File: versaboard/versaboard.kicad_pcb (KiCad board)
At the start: 4 copper layers, 57 x 43 mm, 23 parts, among them J3 UART, J39 Conn_02x20_Odd_Even, J4 DBG, J40 Conn_02x20_Odd_Even, SW1 RST, U1 ATSAML21G18B-AUT, Y1 32.768kHz

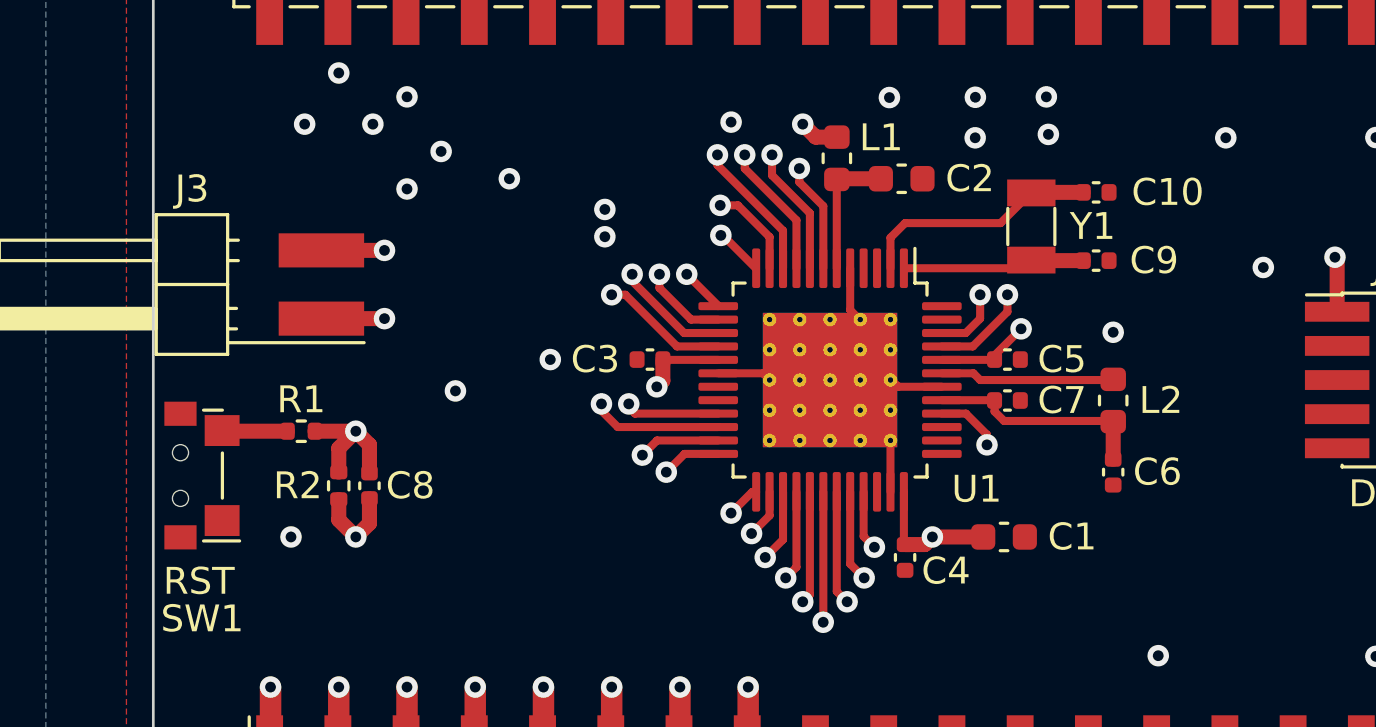
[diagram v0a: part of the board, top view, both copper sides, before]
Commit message: versaboard: geographic reannotate
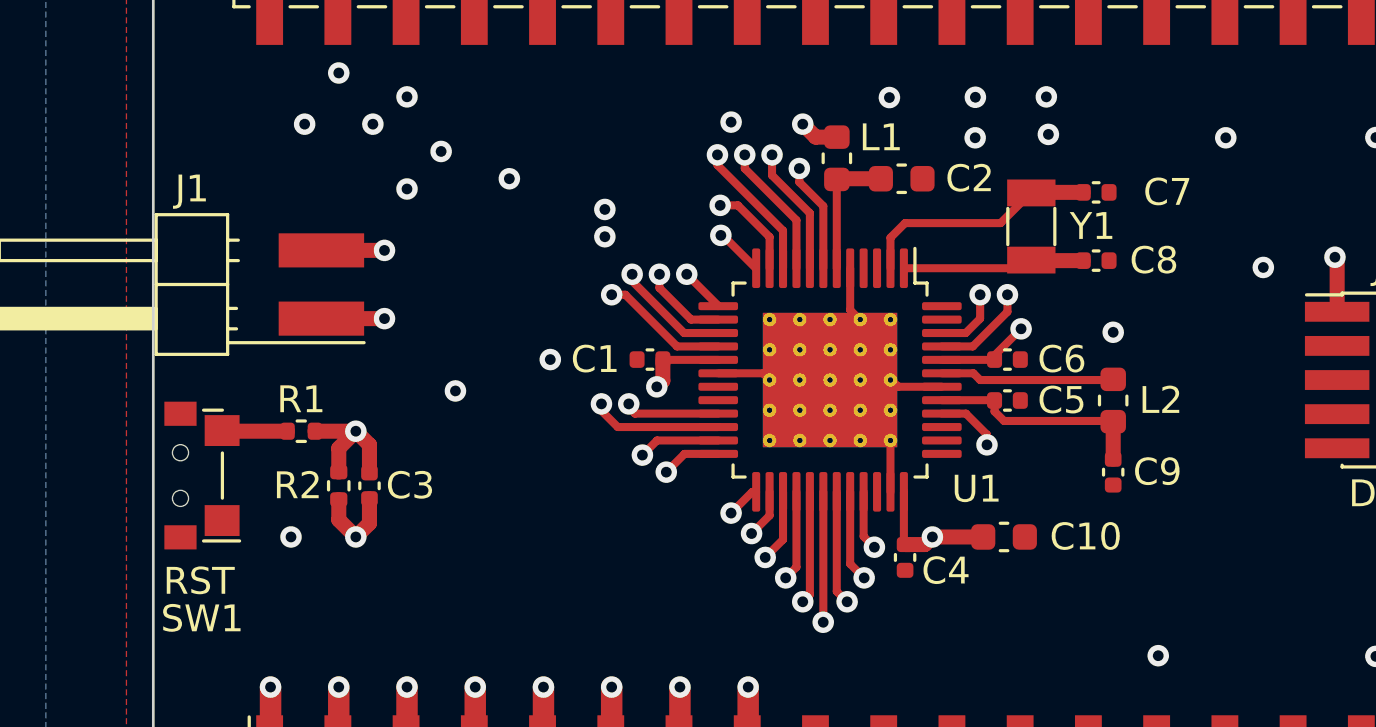
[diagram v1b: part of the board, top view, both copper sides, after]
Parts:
- renumbered C3 to C1, C1 to C10, C8 to C3, C7 to C5, C5 to C6, C10 to C7, C9 to C8, C6 to C9, J3 to J1
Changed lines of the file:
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@@
   (net 27 "/TX")
   (net 28 "/RX")
-  (net 29 "unconnected-(J4-Pad6)")
-  (net 30 "unconnected-(J4-Pad7)")
-  (net 31 "unconnected-(J4-Pad8)")
-  (net 32 "unconnected-(J4-Pad9)")
+  (net 29 "Net-(C5-Pad2)")
+  (net 30 "Net-(C6-Pad2)")
+  (net 31 "unconnected-(J3-Pad6)")
+  (net 32 "unconnected-(J3-Pad7)")
   (net 33 "/VSW")
   (net 34 "Net-(R1-Pad1)")
@@
   (net 43 "unconnected-(U1-Pad47)")
   (net 44 "unconnected-(U1-Pad48)")
-  (net 45 "Net-(C9-Pad2)")
-  (net 46 "Net-(C10-Pad2)")
+  (net 45 "unconnected-(J3-Pad8)")
+  (net 46 "unconnected-(J3-Pad9)")
   (net 47 "/SWDIO")
   (net 48 "/SWCLK")
@@
     (property "Sheetname" "")
     (attr smd)
-    (fp_text reference "C3" (at 2.032 0) (layer "F.SilkS")
+    (fp_text reference "C1" (at 2.032 0) (layer "F.SilkS")
       (effects (font (size 1 1) (thickness 0.15)))
     )
@@
     (property "Sheetname" "")
     (attr smd)
-    (fp_text reference "C7" (at 2.032 0) (layer "F.SilkS")
+    (fp_text reference "C5" (at 2.032 0) (layer "F.SilkS")
       (effects (font (size 1 1) (thickness 0.15)))
     )
@@
     (property "Sheetname" "")
     (attr smd)
-    (fp_text reference "C6" (at 0 -1.651 180) (layer "F.SilkS")
+    (fp_text reference "C9" (at 0 -1.651 180) (layer "F.SilkS")
       (effects (font (size 1 1) (thickness 0.15)))
     )
@@
     (property "Sheetname" "")
     (attr smd)
-    (fp_text reference "C5" (at 2.032 0) (layer "F.SilkS")
+    (fp_text reference "C6" (at 2.032 0) (layer "F.SilkS")
       (effects (font (size 1 1) (thickness 0.15)))
     )
@@
     (property "Sheetname" "")
     (attr smd)
-    (fp_text reference "C8" (at 0 1.524 180) (layer "F.SilkS")
+    (fp_text reference "C3" (at 0 1.524 180) (layer "F.SilkS")
       (effects (font (size 1 1) (thickness 0.15)))
     )
@@
     (fp_line (start 1.6 -0.75) (end 1.6 0.75) (layer "F.Fab") (width 0.1))
     (pad "1" smd rect (at 1.25 0 90) (size 1 1.8) (layers "F.Cu" "F.Paste" "F.Mask")
-      (net 46 "Net-(C10-Pad2)") (pinfunction "1") (pintype "passive"))
+      (net 29 "Net-(C5-Pad2)") (pinfunction "1") (pintype "passive"))
     (pad "2" smd rect (at -1.25 0 90) (size 1 1.8) (layers "F.Cu" "F.Paste" "F.Mask")
-      (net 45 "Net-(C9-Pad2)") (pinfunction "2") (pintype "passive"))
+      (net 30 "Net-(C6-Pad2)") (pinfunction "2") (pintype "passive"))
     (model "${KICAD6_3DMODEL_DIR}/Crystal.3dshapes/Crystal_SMD_3215-2Pin_3.2x1.5mm.wrl"
       (offset (xyz 0 0 0))
@@
     (property "Sheetname" "")
     (attr smd)
-    (fp_text reference "C1" (at 2.54 0 180) (layer "F.SilkS")
+    (fp_text reference "C10" (at 3.048 0 180) (layer "F.SilkS")
       (effects (font (size 1 1) (thickness 0.15)))
     )
@@
     (property "Sheetname" "")
     (attr smd)
-    (fp_text reference "C10" (at -2.667 0) (layer "F.SilkS")
+    (fp_text reference "C7" (at -2.667 0) (layer "F.SilkS")
       (effects (font (size 1 1) (thickness 0.15)))
     )
@@
       (net 1 "GND") (pintype "passive"))
     (pad "2" smd roundrect (at 0.48 0 180) (size 0.56 0.62) (layers "F.Cu" "F.Paste" "F.Mask") (roundrect_rratio 0.25)
-      (net 46 "Net-(C10-Pad2)") (pintype "passive"))
+      (net 29 "Net-(C5-Pad2)") (pintype "passive"))
     (model "${KICAD6_3DMODEL_DIR}/Capacitor_SMD.3dshapes/C_0402_1005Metric.wrl"
       (offset (xyz 0 0 0))
@@
     (property "Sheetname" "")
     (attr smd)
-    (fp_text reference "J3" (at -0.3556 3.556) (layer "F.SilkS")
+    (fp_text reference "J1" (at -0.3556 3.556) (layer "F.SilkS")
       (effects (font (size 1 1) (thickness 0.15)))
     )
@@
     (property "Sheetname" "")
     (attr smd)
-    (fp_text reference "C9" (at -2.159 0) (layer "F.SilkS")
+    (fp_text reference "C8" (at -2.159 0) (layer "F.SilkS")
       (effects (font (size 1 1) (thickness 0.15)))
     )
@@
       (net 1 "GND") (pintype "passive"))
     (pad "2" smd roundrect (at 0.48 0 180) (size 0.56 0.62) (layers "F.Cu" "F.Paste" "F.Mask") (roundrect_rratio 0.25)
-      (net 45 "Net-(C9-Pad2)") (pintype "passive"))
+      (net 30 "Net-(C6-Pad2)") (pintype "passive"))
     (model "${KICAD6_3DMODEL_DIR}/Capacitor_SMD.3dshapes/C_0402_1005Metric.wrl"
       (offset (xyz 0 0 0))
@@
       (net 1 "GND") (pinfunction "Pin_5") (pintype "passive"))
     (pad "6" smd rect (at 1.95 0) (size 2.4 0.74) (layers "F.Cu" "F.Paste" "F.Mask")
-      (net 29 "unconnected-(J4-Pad6)") (pinfunction "Pin_6") (pintype "passive+no_connect"))
+      (net 31 "unconnected-(J3-Pad6)") (pinfunction "Pin_6") (pintype "passive+no_connect"))
     (pad "7" smd rect (at -1.95 1.27) (size 2.4 0.74) (layers "F.Cu" "F.Paste" "F.Mask")
-      (net 30 "unconnected-(J4-Pad7)") (pinfunction "Pin_7") (pintype "passive+no_connect"))
+      (net 32 "unconnected-(J3-Pad7)") (pinfunction "Pin_7") (pintype "passive+no_connect"))
     (pad "8" smd rect (at 1.95 1.27) (size 2.4 0.74) (layers "F.Cu" "F.Paste" "F.Mask")
-      (net 31 "unconnected-(J4-Pad8)") (pinfunction "Pin_8") (pintype "passive+no_connect"))
+      (net 45 "unconnected-(J3-Pad8)") (pinfunction "Pin_8") (pintype "passive+no_connect"))
     (pad "9" smd rect (at -1.95 2.54) (size 2.4 0.74) (layers "F.Cu" "F.Paste" "F.Mask")
-      (net 32 "unconnected-(J4-Pad9)") (pinfunction "Pin_9") (pintype "passive+no_connect"))
+      (net 46 "unconnected-(J3-Pad9)") (pinfunction "Pin_9") (pintype "passive+no_connect"))
     (pad "10" smd rect (at 1.95 2.54) (size 2.4 0.74) (layers "F.Cu" "F.Paste" "F.Mask")
       (net 107 "/~{RST}") (pinfunction "Pin_10") (pintype "passive"))
@@
       ))
     (pad "1" smd roundrect (at -4.1625 -2.75 270) (size 1.475 0.3) (layers "F.Cu" "F.Paste" "F.Mask") (roundrect_rratio 0.25)
-      (net 45 "Net-(C9-Pad2)") (pinfunction "PA00") (pintype "bidirectional"))
+      (net 30 "Net-(C6-Pad2)") (pinfunction "PA00") (pintype "bidirectional"))
     (pad "2" smd roundrect (at -4.1625 -2.25 270) (size 1.475 0.3) (layers "F.Cu" "F.Paste" "F.Mask") (roundrect_rratio 0.25)
-      (net 46 "Net-(C10-Pad2)") (pinfunction "PA01") (pintype "bidirectional"))
+      (net 29 "Net-(C5-Pad2)") (pinfunction "PA01") (pintype "bidirectional"))
     (pad "3" smd roundrect (at -4.1625 -1.75 270) (size 1.475 0.3) (layers "F.Cu" "F.Paste" "F.Mask") (roundrect_rratio 0.25)
       (net 36 "unconnected-(U1-Pad3)") (pinfunction "PA02") (pintype "bidirectional+no_connect"))
@@
   (segment (start 49.31 55.89) (end 46.897 55.89) (width 0.56) (layer "In2.Cu") (net 28))
   (segment (start 45.373 57.414) (end 41.1058 57.414) (width 0.56) (layer "In2.Cu") (net 28))
+  (segment (start 64.042 56.398) (end 65.185 55.255) (width 0.3) (layer "F.Cu") (net 29))
+  (segment (start 59.942 56.942) (end 60.486 56.398) (width 0.3) (layer "F.Cu") (net 29))
+  (segment (start 67.118 55.255) (end 65.185 55.255) (width 0.56) (layer "F.Cu") (net 29))
+  (segment (start 59.942 58.0775) (end 59.942 56.942) (width 0.3) (layer "F.Cu") (net 29))
+  (segment (start 60.486 56.398) (end 64.042 56.398) (width 0.3) (layer "F.Cu") (net 29))
+  (segment (start 60.442 58.0775) (end 64.9025 58.0775) (width 0.3) (layer "F.Cu") (net 30))
+  (segment (start 67.118 57.795) (end 65.185 57.795) (width 0.56) (layer "F.Cu") (net 30))
   (segment (start 63.28 62.24) (end 68.233 62.24) (width 0.3) (layer "F.Cu") (net 33))
   (segment (start 63.03 61.99) (end 63.28 62.24) (width 0.3) (layer "F.Cu") (net 33))
@@
   (segment (start 59.343 68.463) (end 60.105 69.225) (width 0.56) (layer "In1.Cu") (net 35))
   (segment (start 80.8695 69.225) (end 82.2665 67.828) (width 0.56) (layer "In1.Cu") (net 35))
-  (segment (start 60.442 58.0775) (end 64.9025 58.0775) (width 0.3) (layer "F.Cu") (net 45))
-  (segment (start 67.118 57.795) (end 65.185 57.795) (width 0.56) (layer "F.Cu") (net 45))
-  (segment (start 64.042 56.398) (end 65.185 55.255) (width 0.3) (layer "F.Cu") (net 46))
-  (segment (start 59.942 56.942) (end 60.486 56.398) (width 0.3) (layer "F.Cu") (net 46))
-  (segment (start 67.118 55.255) (end 65.185 55.255) (width 0.56) (layer "F.Cu") (net 46))
-  (segment (start 59.942 58.0775) (end 59.942 56.942) (width 0.3) (layer "F.Cu") (net 46))
-  (segment (start 60.486 56.398) (end 64.042 56.398) (width 0.3) (layer "F.Cu") (net 46))
   (segment (start 61.8545 60.49) (end 62.744 60.49) (width 0.3) (layer "F.Cu") (net 47))
   (segment (start 80.47 59.7) (end 83.346 59.7) (width 0.56) (layer "F.Cu") (net 47))
